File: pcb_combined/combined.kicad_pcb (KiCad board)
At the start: 2 copper layers, 57.2 x 40.1 mm, 20 parts, among them J1 Cable, J1 Pins, J2 Floppy, J2 Socket, J3 CFG1, J4 CFG2, J5 CFG3, J6 UPDI, Q1 DMG2301L, Q2 BSS123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

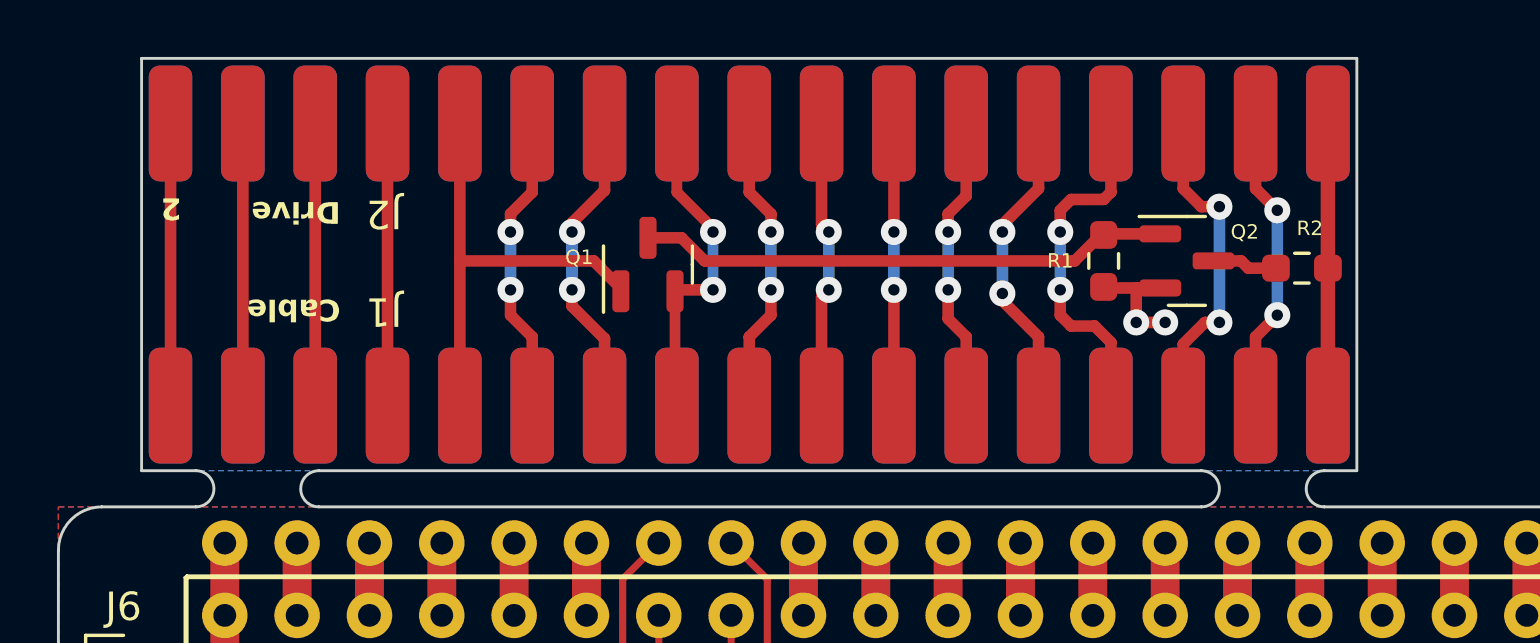
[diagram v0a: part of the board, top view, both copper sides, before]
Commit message: Combined PCB: redone to fix silk screen labels orientation
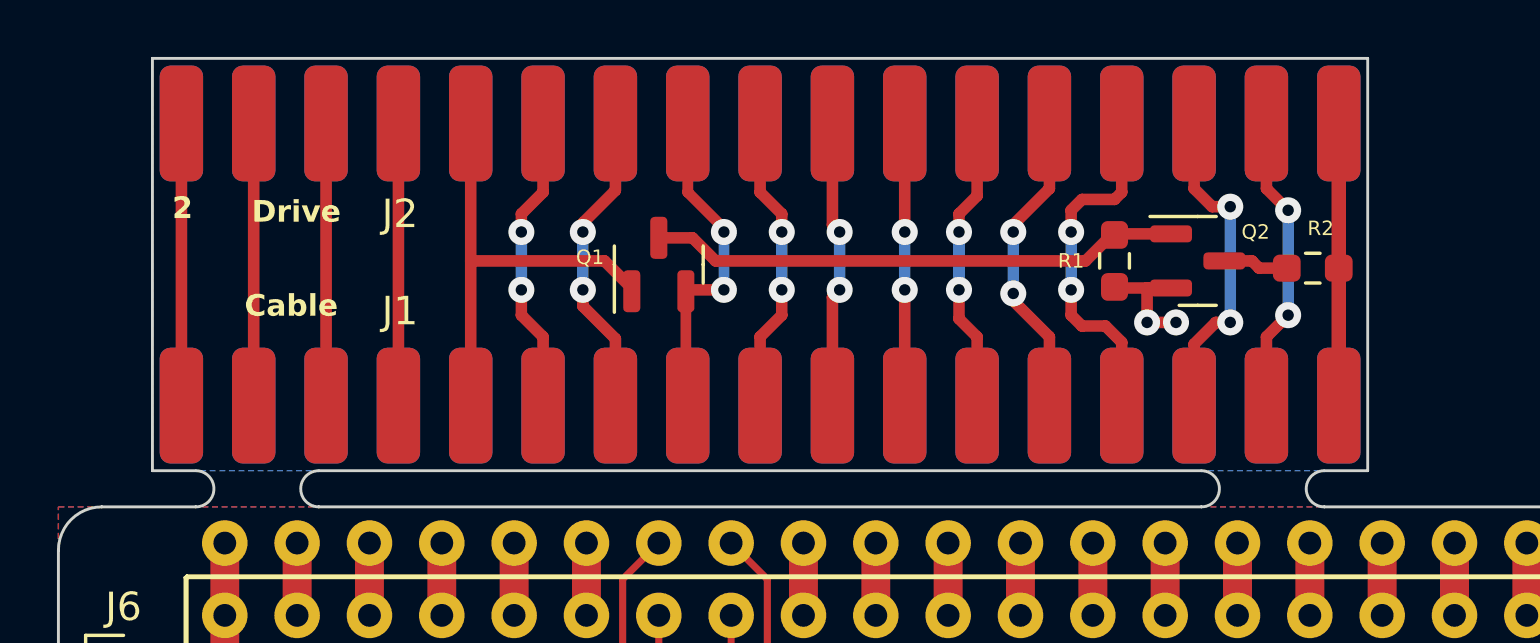
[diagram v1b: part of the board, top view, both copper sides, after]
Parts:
- moved J1 0.38 mm to (29.5, 36.3)
- moved J2 0.38 mm to (29.5, 26.4)
- moved Q1 0.38 mm to (46.2, 31.4)
- moved Q2 0.38 mm to (65.2, 31.2)
- moved R1 0.38 mm to (62.2, 31.2)
- moved R2 0.38 mm to (69.2, 31.5)
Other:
- outline, holes or cut-outs redrawn

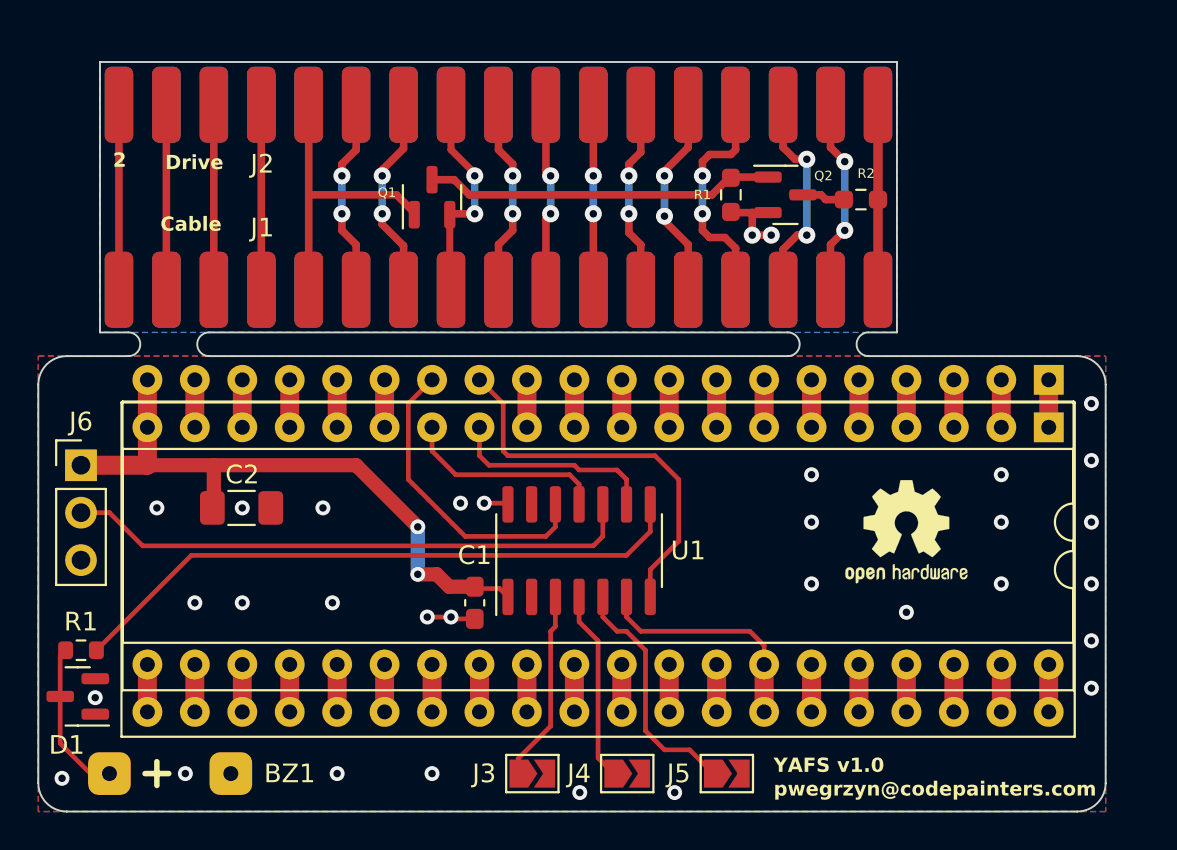
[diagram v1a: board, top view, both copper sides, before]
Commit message: Combined PCB - larger slot, as per JLCPCB request.
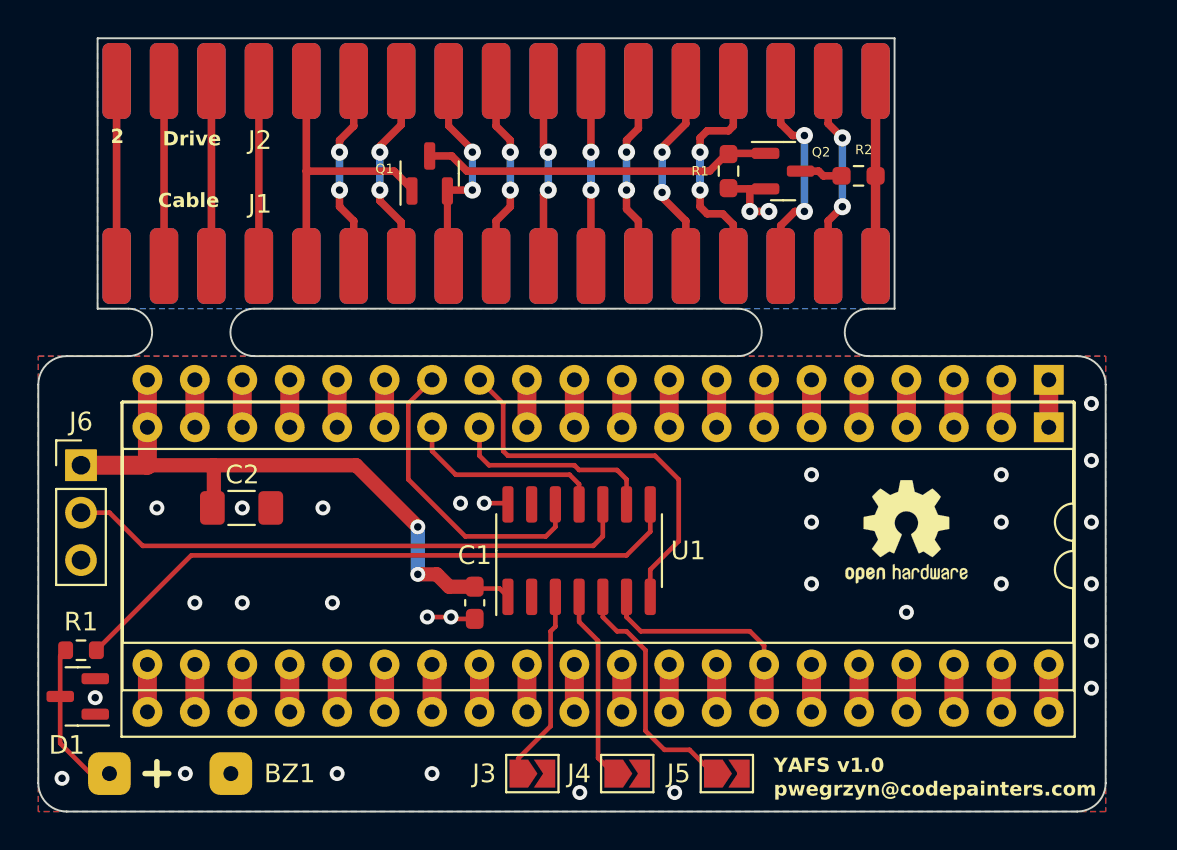
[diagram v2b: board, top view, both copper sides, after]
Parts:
- moved J1 1.28 mm to (29.3, 35.1)
- moved R2 1.28 mm to (69.1, 30.2)
- moved Q1 1.28 mm to (46.1, 30.1)
- moved J2 1.28 mm to (29.3, 25.1)
- moved Q2 1.28 mm to (65.0, 30.0)
- moved R1 1.28 mm to (62.1, 30.0)
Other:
- board size 57.2 x 40.1 mm -> 57.2 x 41.4 mm
